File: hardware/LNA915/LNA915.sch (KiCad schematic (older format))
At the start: 34 parts, among them P1 HACKRF, P2 ANTENNA, P3 CONN_1, P4 CONN_1, U1 SWITCH, U2 SAW, U3 LNA

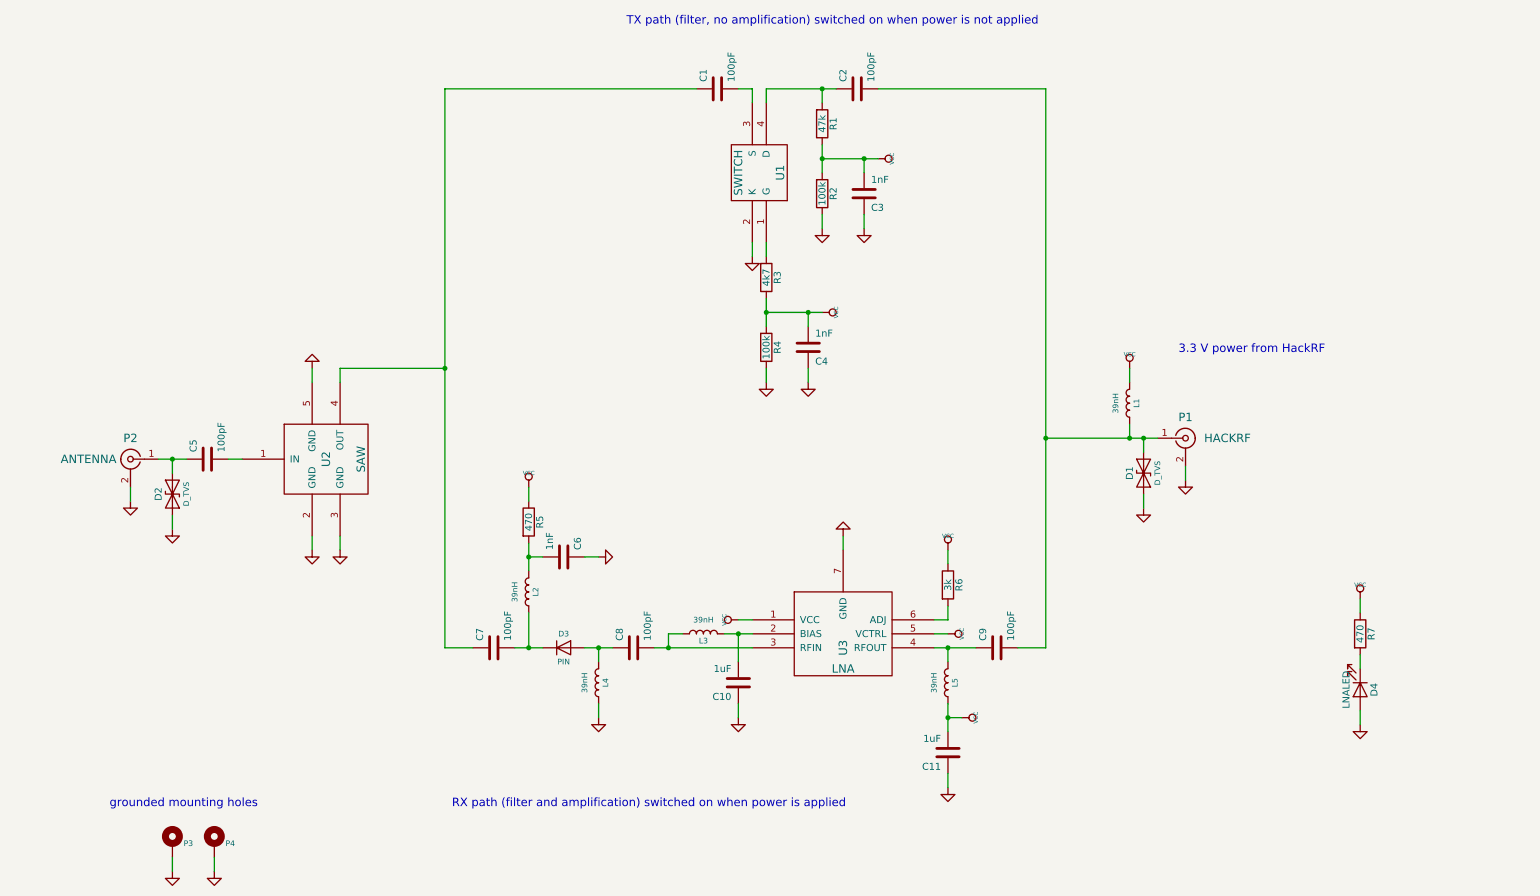
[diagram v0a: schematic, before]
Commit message: LNA915: redesign around GRF6011 failsafe switch
fits in SMA-KIT-1.5MF inline SMA enclosure
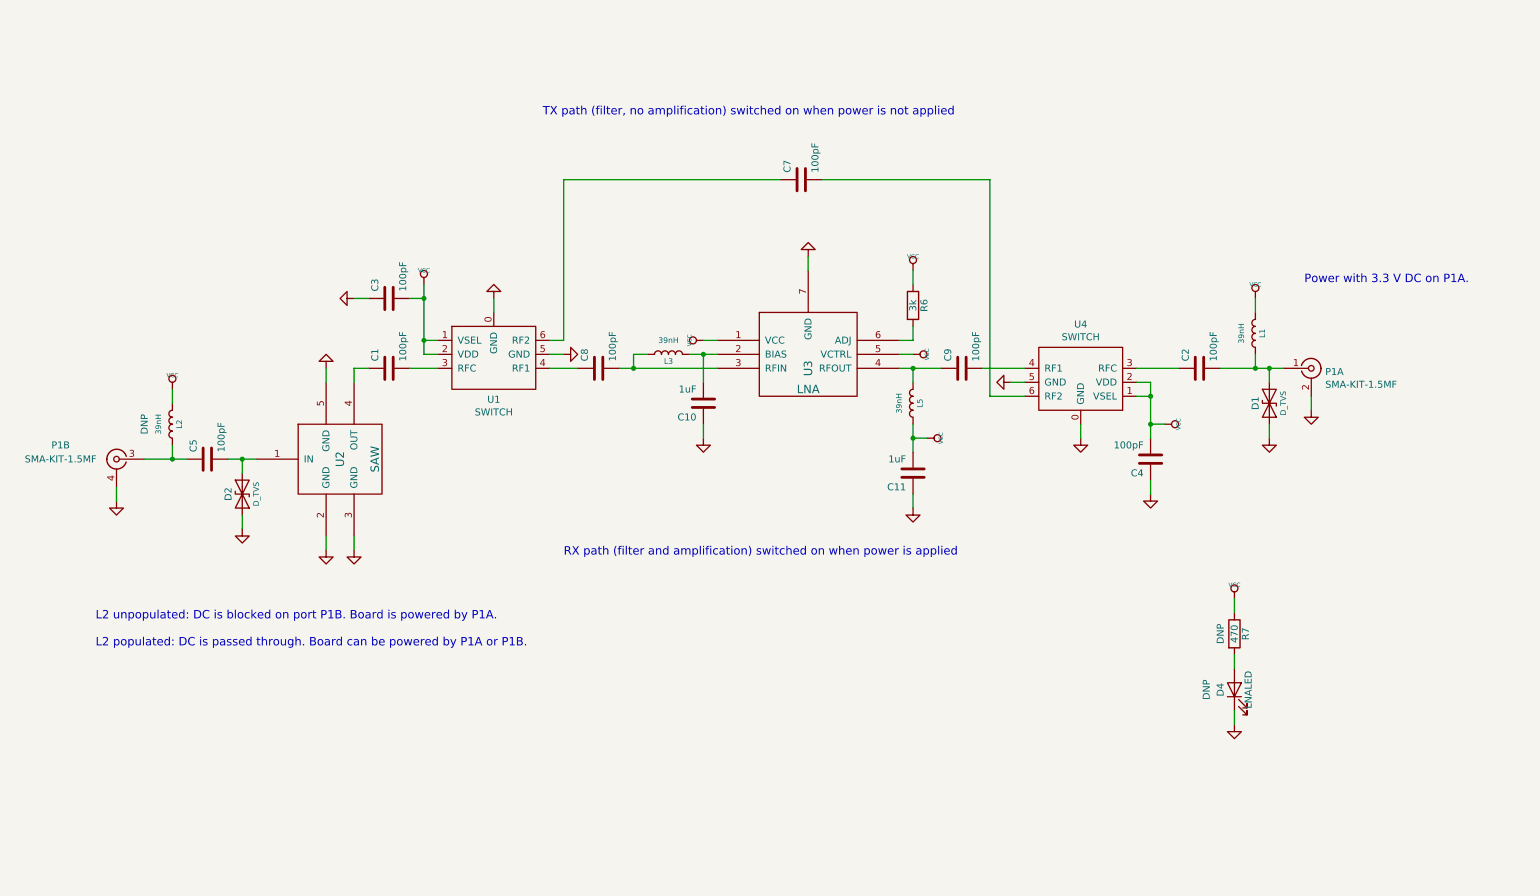
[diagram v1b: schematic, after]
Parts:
- removed C6: 1nF, gsg-modules:0402, symbol Device:C
- removed D3: PIN, hackrf:GSG-SOD323, symbol Device:D
- removed L4: 39nH, gsg-modules:0402, symbol Device:L
- removed P1: HACKRF, gsg-modules:SMA-EDGE, symbol Connector:Conn_Coaxial
- removed P2: ANTENNA, gsg-modules:SMA-EDGE, symbol Connector:Conn_Coaxial
- removed P3, P4: CONN_1, hackrf:GSG-HOLE-62MIL-COPPER, symbol Mechanical:MountingHole_Pad
- removed R1: 47k, gsg-modules:0402, symbol Device:R
- removed R2, R4: 100k, gsg-modules:0402, symbol Device:R
- removed R3: 4k7, gsg-modules:0402, symbol Device:R
- removed R5: 470, gsg-modules:0402, symbol Device:R
- removed U1: SWITCH, hackrf:GSG-SOT143, symbol hackrf:BF1118
- added P1: SMA-KIT-1.5MF, LNA915:SMA-KIT-1.5MF, symbol LNA915:SMA-KIT-1.5MF
- added U1, U4: SWITCH, LNA915:GRF6011, symbol LNA915:GRF6011
- C1, C2, C5, C7, C8, C9: Part Number GRM1555C1H101JA01D -> GCM1555C1H101JA16
- C3, C4: value 1nF -> 100pF; Description CAP CER 1000PF 50V 10% X7R 0402 -> CAP CER 100PF 50V 5% NP0 0402; Part Number GRM155R71H102KA01D -> GCM1555C1H101JA16
- D1, D2: Description TVS DIODE ESD .05PF 15KV 0402 -> TVS DIODE 4V 1005; Part Number LXES15AAA1-100 -> LXES15AAA1-153
- D4: footprint gsg-modules:0603D -> gsg-modules:0402; Description LED GREEN STD BRIGHT 0603 SMD -> (none); Manufacturer Everlight -> (none); Note (none) -> DNP; Part Number QTLP601C4TR -> (none)
- L2, R7: Note (none) -> DNP
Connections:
- net GND: now also D4.1 (K), P1.2 (SHIELD), P1.4 (SHIELD), U1.0 (GND), U1.5 (GND), U4.0 (GND), U4.5 (GND); no longer D4.2 (A)
- net VCC: now also L2.2, U1.1 (VSEL), U1.2 (VDD), U4.1 (VSEL), U4.2 (VDD)
- net at L2.1: now also C5.1, P1.3 (RF); no longer C7.2
- net at C8.1: now also U1.4 (RF1)
- net at C2.2, D1.2 (A2), L1.1: now also P1.1 (RF); no longer C9.2
- net at D2.2 (A2): now also C5.2, U2.1 (IN); no longer C5.1
- net at C1.1, U2.4 (OUT): no longer C7.1
- net at R7.2: now also D4.2 (A); no longer D4.1 (K)
- net at C1.2: now also U1.3 (RFC)
- net at C2.1: now also U4.3 (RFC)
- new net: C7.1, U1.6 (RF2)
- new net: C7.2, U4.6 (RF2)
- new net: C9.2, U4.4 (RF1)
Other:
- note added: "L2 unpopulated: DC is blocked on port P1B. Board is powered by P1A.\n\nL2 populated: DC is passed through. Board can be powered by P1A or P1B."
- note added: "Power with 3.3 V DC on P1A."
- note removed: "3.3 V power from HackRF"
- note removed: "grounded mounting holes"
- moved on the sheet: C1, C10, C11, C2, C7, C8, C9, D1, D2, D4, L1, L3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

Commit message: LNA915: make easier to assemble
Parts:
- U2: footprint hackrf:GSG-F5Q -> LNA915:F5Q
- U3: footprint hackrf:GSG-TSLP-7-1 -> LNA915:TSLP-7-1
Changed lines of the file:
@@
 F 0 "U2" V 2900 3900 60  0000 C CNN
 F 1 "SAW" V 3150 3900 60  0000 C CNN
-F 2 "hackrf:GSG-F5Q" H 2900 3900 60  0001 C CNN
+F 2 "LNA915:F5Q" H 2900 3900 60  0001 C CNN
 F 3 "~" H 2900 3900 60  0000 C CNN
 F 4 "Taiyo Yuden" H 2900 3900 60  0001 C CNN "Manufacturer"
@@
 F 0 "U3" V 6250 3050 60  0000 C CNN
 F 1 "LNA" H 6250 2900 60  0000 C CNN
-F 2 "hackrf:GSG-TSLP-7-1" H 6250 3150 60  0001 C CNN
+F 2 "LNA915:TSLP-7-1" H 6250 3150 60  0001 C CNN
 F 3 "~" H 6250 3150 60  0000 C CNN
 F 4 "Infineon" H 6250 3150 60  0001 C CNN "Manufacturer"

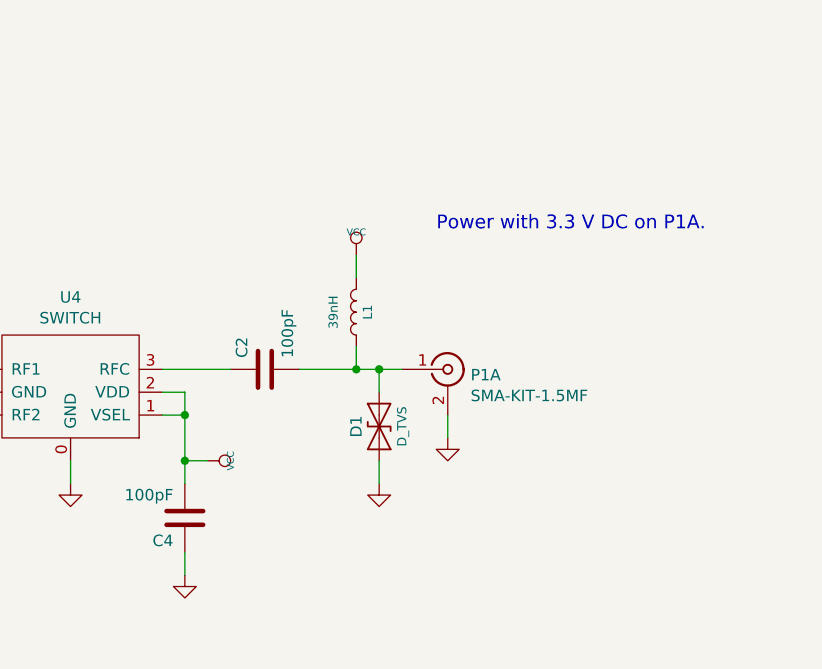
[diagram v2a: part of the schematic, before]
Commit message: LNA915: add optional shunt capacitor
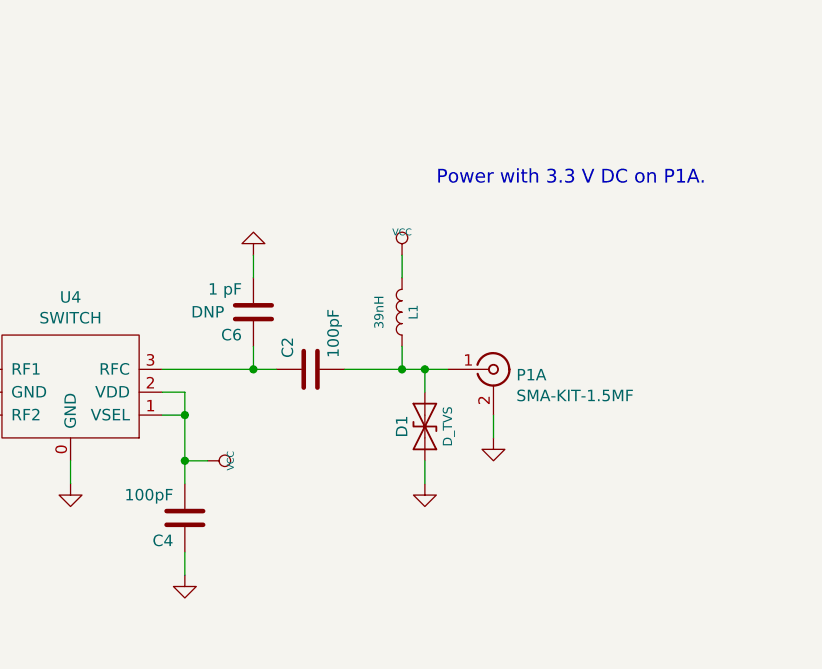
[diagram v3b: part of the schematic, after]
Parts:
- added C6: 1 pF, gsg-modules:0402, symbol Device:C
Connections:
- net GND: now also C6.2
- net at C2.1, U4.3 (RFC): now also C6.1
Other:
- moved on the sheet: C2, D1, L1, P1A
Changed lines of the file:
@@
 L Device:D_TVS D1
 U 1 1 52F44107
-P 9550 3500
-F 0 "D1" H 9550 3600 50  0000 C CNN
-F 1 "D_TVS" H 9550 3400 40  0000 C CNN
-F 2 "gsg-modules:0402" H 9550 3500 60  0001 C CNN
-F 3 "~" H 9550 3500 60  0000 C CNN
-F 4 "Murata" H 9550 3500 60  0001 C CNN "Manufacturer"
-F 5 "LXES15AAA1-153" H 9550 3500 60  0001 C CNN "Part Number"
-F 6 "TVS DIODE 4V 1005" H 9550 3500 60  0001 C CNN "Description"
-	1    9550 3500
+P 9750 3500
+F 0 "D1" H 9750 3600 50  0000 C CNN
+F 1 "D_TVS" H 9750 3400 40  0000 C CNN
+F 2 "gsg-modules:0402" H 9750 3500 60  0001 C CNN
+F 3 "~" H 9750 3500 60  0000 C CNN
+F 4 "Murata" H 9750 3500 60  0001 C CNN "Manufacturer"
+F 5 "LXES15AAA1-153" H 9750 3500 60  0001 C CNN "Part Number"
+F 6 "TVS DIODE 4V 1005" H 9750 3500 60  0001 C CNN "Description"
+	1    9750 3500
 	0    -1   -1   0
 $EndComp
@@
 L power:GND #PWR01
 U 1 1 52F44137
-P 9850 3550
-F 0 "#PWR01" H 9850 3550 30  0001 C CNN
-F 1 "GND" H 9850 3480 30  0001 C CNN
-F 2 "" H 9850 3550 50  0001 C CNN
-F 3 "" H 9850 3550 50  0001 C CNN
-	1    9850 3550
+P 10050 3550
+F 0 "#PWR01" H 10050 3550 30  0001 C CNN
+F 1 "GND" H 10050 3480 30  0001 C CNN
+F 2 "" H 10050 3550 50  0001 C CNN
+F 3 "" H 10050 3550 50  0001 C CNN
+	1    10050 3550
 	1    0    0    -1
 $EndComp
@@
 L power:GND #PWR02
 U 1 1 52F44144
-P 9550 3750
-F 0 "#PWR02" H 9550 3750 30  0001 C CNN
-F 1 "GND" H 9550 3680 30  0001 C CNN
-F 2 "" H 9550 3750 50  0001 C CNN
-F 3 "" H 9550 3750 50  0001 C CNN
-	1    9550 3750
-	1    0    0    -1
-$EndComp
-Wire Wire Line
-	9550 3650 9550 3750
-Wire Wire Line
-	9850 3450 9850 3550
-Wire Wire Line
-	9550 3250 9550 3350
+P 9750 3750
+F 0 "#PWR02" H 9750 3750 30  0001 C CNN
+F 1 "GND" H 9750 3680 30  0001 C CNN
+F 2 "" H 9750 3750 50  0001 C CNN
+F 3 "" H 9750 3750 50  0001 C CNN
+	1    9750 3750
+	1    0    0    -1
+$EndComp
+Wire Wire Line
+	9750 3650 9750 3750
+Wire Wire Line
+	10050 3450 10050 3550
+Wire Wire Line
+	9750 3250 9750 3350
 $Comp
 L power:GND #PWR03
@@
 	0    -1   -1   0
 $EndComp
-Connection ~ 9550 3250
-Wire Wire Line
-	9450 3150 9450 3250
-Connection ~ 9450 3250
+Connection ~ 9750 3250
+Wire Wire Line
+	9650 3150 9650 3250
+Connection ~ 9650 3250
 Connection ~ 2200 3900
 $Comp
@@
 Wire Wire Line
 	9300 5700 9300 5800
-Text Notes 9800 2650 0    60   ~ 0
+Text Notes 9800 2450 0    60   ~ 0
 Power with 3.3 V DC on P1A.
 Wire Wire Line
-	9200 3250 9450 3250
+	9400 3250 9650 3250
 Wire Wire Line
 	3400 3250 3600 3250
@@
 	9300 5300 9300 5400
 Wire Wire Line
-	9550 3250 9650 3250
-Wire Wire Line
-	9450 3250 9550 3250
+	9750 3250 9850 3250
+Wire Wire Line
+	9650 3250 9750 3250
 Wire Wire Line
 	2200 3900 2300 3900
@@
 L Device:C C2
 U 1 1 52F69EC3
-P 9050 3250
-F 0 "C2" H 9100 3350 50  0000 L CNN
-F 1 "100pF" H 9100 3150 50  0000 L CNN
-F 2 "gsg-modules:0402" H 9050 3250 50  0001 C CNN
-F 3 "" H 9050 3250 50  0001 C CNN
-F 4 "Murata" H 9050 3250 60  0001 C CNN "Manufacturer"
-F 5 "GCM1555C1H101JA16" H 9050 3250 60  0001 C CNN "Part Number"
-F 6 "CAP CER 100PF 50V 5% NP0 0402" H 9050 3250 60  0001 C CNN "Description"
-	1    9050 3250
+P 9250 3250
+F 0 "C2" H 9300 3350 50  0000 L CNN
+F 1 "100pF" H 9300 3150 50  0000 L CNN
+F 2 "gsg-modules:0402" H 9250 3250 50  0001 C CNN
+F 3 "" H 9250 3250 50  0001 C CNN
+F 4 "Murata" H 9250 3250 60  0001 C CNN "Manufacturer"
+F 5 "GCM1555C1H101JA16" H 9250 3250 60  0001 C CNN "Part Number"
+F 6 "CAP CER 100PF 50V 5% NP0 0402" H 9250 3250 60  0001 C CNN "Description"
+	1    9250 3250
 	0    -1   -1   0
 $EndComp
@@
 	3000 3250 3100 3250
 Wire Wire Line
-	8600 3250 8900 3250
+	8600 3250 9000 3250
 $Comp
 L power:VCC #PWR0101
@@
 	1500 3900 1700 3900
 Wire Wire Line
-	9450 2750 9450 2850
+	9650 2750 9650 2850
 $Comp
 L power:VCC #PWR015
 U 1 1 52F68C7C
-P 9450 2750
-F 0 "#PWR015" H 9450 2850 30  0001 C CNN
-F 1 "VCC" H 9450 2850 30  0000 C CNN
-F 2 "" H 9450 2750 50  0001 C CNN
-F 3 "" H 9450 2750 50  0001 C CNN
-	1    9450 2750
+P 9650 2750
+F 0 "#PWR015" H 9650 2850 30  0001 C CNN
+F 1 "VCC" H 9650 2850 30  0000 C CNN
+F 2 "" H 9650 2750 50  0001 C CNN
+F 3 "" H 9650 2750 50  0001 C CNN
+	1    9650 2750
 	1    0    0    -1
 $EndComp
@@
 L Device:L L1
 U 1 1 52F68C64
-P 9450 3000
-F 0 "L1" V 9400 3000 40  0000 C CNN
-F 1 "39nH" V 9550 3000 40  0000 C CNN
-F 2 "gsg-modules:0402" H 9450 3000 50  0001 C CNN
-F 3 "" H 9450 3000 50  0001 C CNN
-F 4 "Taiyo Yuden" H 9450 3000 60  0001 C CNN "Manufacturer"
-F 5 "HK100539NJ-T" H 9450 3000 60  0001 C CNN "Part Number"
-F 6 "INDUCTOR HI FREQ 39NH 5% 0402" H 9450 3000 60  0001 C CNN "Description"
-	1    9450 3000
+P 9650 3000
+F 0 "L1" V 9600 3000 40  0000 C CNN
+F 1 "39nH" V 9750 3000 40  0000 C CNN
+F 2 "gsg-modules:0402" H 9650 3000 50  0001 C CNN
+F 3 "" H 9650 3000 50  0001 C CNN
+F 4 "Taiyo Yuden" H 9650 3000 60  0001 C CNN "Manufacturer"
+F 5 "HK100539NJ-T" H 9650 3000 60  0001 C CNN "Part Number"
+F 6 "INDUCTOR HI FREQ 39NH 5% 0402" H 9650 3000 60  0001 C CNN "Description"
+	1    9650 3000
 	-1   0    0    1
 $EndComp
@@
 L LNA915:SMA-KIT-1.5MF P1
 U 1 1 5EF2AE41
-P 9850 3250
-F 0 "P1" H 9950 3225 50  0000 L CNN
-F 1 "SMA-KIT-1.5MF" H 9950 3134 50  0000 L CNN
-F 2 "LNA915:SMA-KIT-1.5MF" H 9850 3250 50  0001 C CNN
-F 3 "" H 9850 3250 50  0001 C CNN
-F 4 "HOUSING BRASS 0.43\"DIA X 1.5\"L" H 9850 3250 50  0001 C CNN "Description"
-F 5 "Crystek" H 9850 3250 50  0001 C CNN "Manufacturer"
-F 6 "SMA-KIT-1.5MF" H 9850 3250 50  0001 C CNN "Part Number"
-	1    9850 3250
+P 10050 3250
+F 0 "P1" H 10150 3225 50  0000 L CNN
+F 1 "SMA-KIT-1.5MF" H 10150 3134 50  0000 L CNN
+F 2 "LNA915:SMA-KIT-1.5MF" H 10050 3250 50  0001 C CNN
+F 3 "" H 10050 3250 50  0001 C CNN
+F 4 "HOUSING BRASS 0.43\"DIA X 1.5\"L" H 10050 3250 50  0001 C CNN "Description"
+F 5 "Crystek" H 10050 3250 50  0001 C CNN "Manufacturer"
+F 6 "SMA-KIT-1.5MF" H 10050 3250 50  0001 C CNN "Part Number"
+	1    10050 3250
 	1    0    0    -1
 $EndComp
@@
 	-1   0    0    -1
 $EndComp
+$Comp
+L Device:C C6
+U 1 1 5F2886C8
+P 9000 3000
+F 0 "C6" H 9050 3100 50  0000 L CNN
+F 1 "1 pF" H 9050 2900 50  0000 L CNN
+F 2 "gsg-modules:0402" H 9000 3000 50  0001 C CNN
+F 3 "" H 9000 3000 50  0001 C CNN
+F 4 "" H 9000 3000 60  0001 C CNN "Manufacturer"
+F 5 "" H 9000 3000 60  0001 C CNN "Part Number"
+F 6 "" H 9000 3000 60  0001 C CNN "Description"
+F 7 "DNP" H 9200 3000 50  0000 C CNN "Note"
+	1    9000 3000
+	-1   0    0    1
+$EndComp
+$Comp
+L power:GND #PWR018
+U 1 1 5F29CA02
+P 9000 2750
+F 0 "#PWR018" H 9000 2750 30  0001 C CNN
+F 1 "GND" H 9000 2680 30  0001 C CNN
+F 2 "" H 9000 2750 50  0001 C CNN
+F 3 "" H 9000 2750 50  0001 C CNN
+	1    9000 2750
+	-1   0    0    1
+$EndComp
+Wire Wire Line
+	9000 2750 9000 2850
+Wire Wire Line
+	9000 3150 9000 3250
+Connection ~ 9000 3250
+Wire Wire Line
+	9000 3250 9100 3250
 $EndSCHEMATC
